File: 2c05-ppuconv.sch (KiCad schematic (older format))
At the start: 6 parts, among them J1 Conn_01x03_Male, J2 Conn_01x02_Male, J3 Conn_01x01_Female, U1 74AHCT1G02, U2 74AHCT1G86

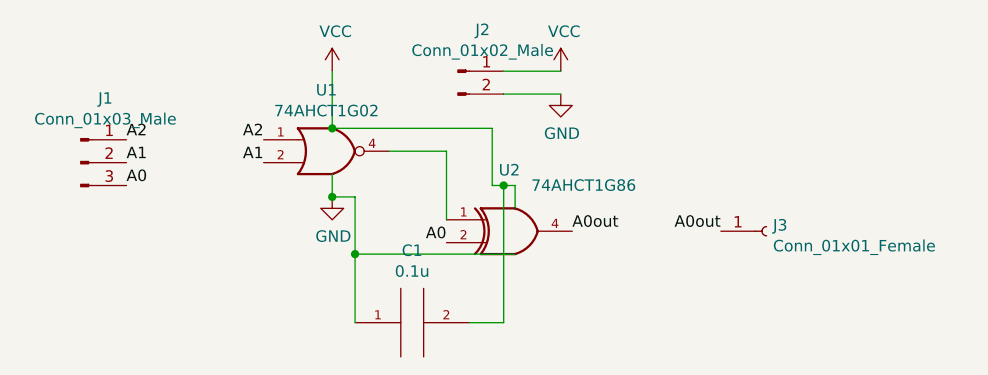
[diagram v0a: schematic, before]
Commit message: update documentation, swap A0 and out pins on PCB, shrink PCB
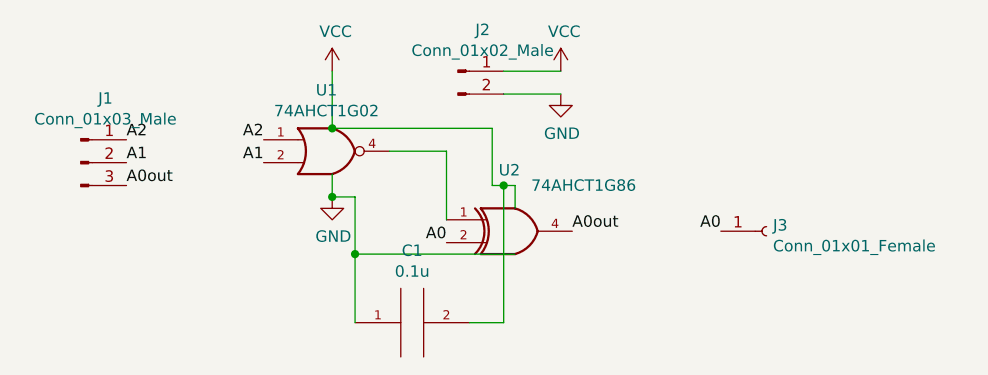
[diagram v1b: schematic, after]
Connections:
- net A0: now also J3.1 (Pin_1); no longer J1.3 (Pin_3)
- net A0out: now also J1.3 (Pin_3); no longer J3.1 (Pin_1)
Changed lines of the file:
@@
 A1
 Text Label 4050 4400 0    50   ~ 0
-A0
+A0out
 $Comp
 L 74xGxx:74AHCT1G02 U1
@@
 $EndComp
 Text Label 6650 4600 2    50   ~ 0
-A0out
+A0
 $EndSCHEMATC
